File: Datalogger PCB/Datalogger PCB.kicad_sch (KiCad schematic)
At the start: 45 parts, among them J1 Conn_01x02_Pin, M1 Motor_Servo, M2 Motor_Servo, M3 Motor_Servo, M4 Motor_Servo, U1 Teensy4.1, U2 BNO055, U3 LPS25HB, U4 AMS1117-5.0, U5 NRF24L01_Breakout, U6 VN5E160STR-E, U7 VN5E160STR-E, U8 VN5E160STR-E, U9 VN5E160STR-E

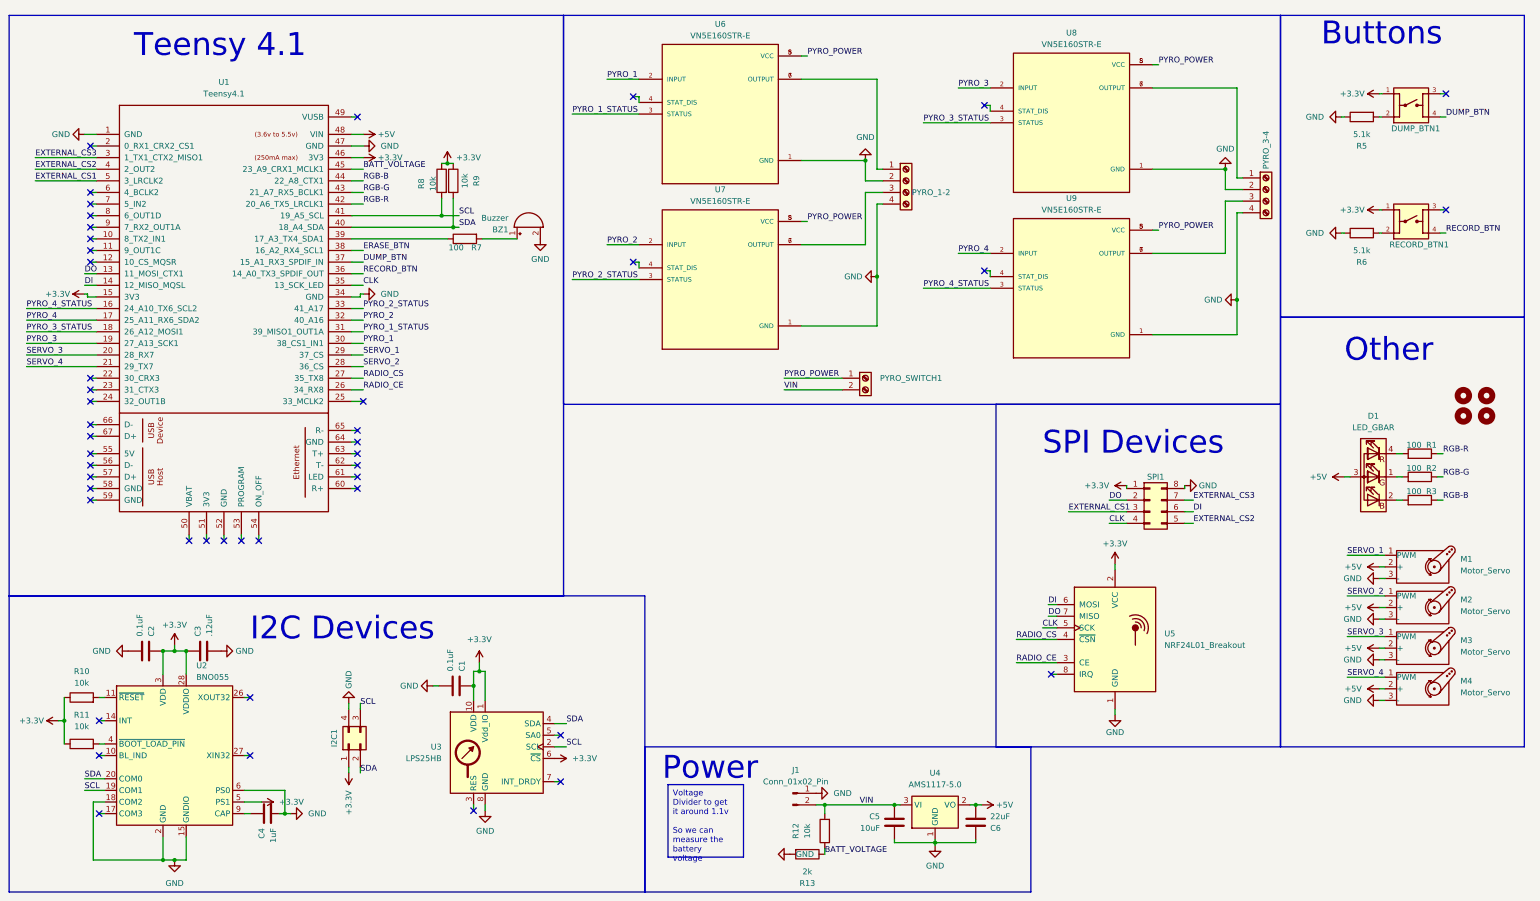
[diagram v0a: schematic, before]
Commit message: Added serial connector and power connectors
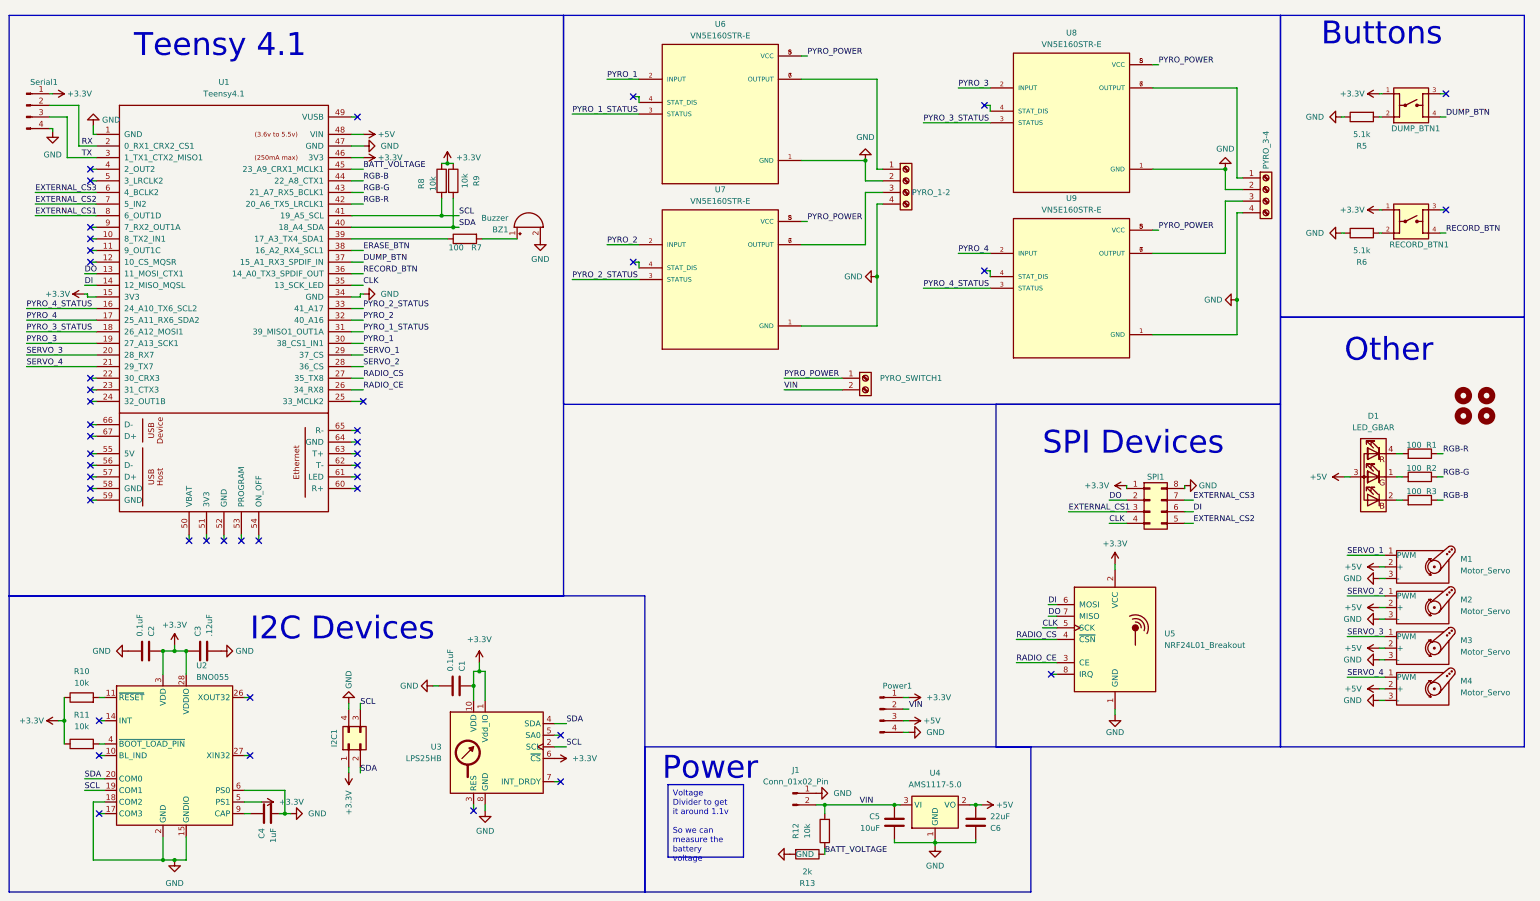
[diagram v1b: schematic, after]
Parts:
- added Power1, Serial1: Conn_01x04_Pin, Connector_PinHeader_1.27mm:PinHeader_1x04_P1.27mm_Vertical, symbol Connector:Conn_01x04_Pin
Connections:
- net +3.3V: now also Power1.1 (Pin_1), Serial1.1 (Pin_1)
- net +5V: now also Power1.3 (Pin_3)
- net EXTERNAL_CS1: now also U1.8 (6_OUT1D); no longer U1.5 (3_LRCLK2)
- net EXTERNAL_CS2: now also U1.7 (5_IN2); no longer U1.4 (2_OUT2)
- net EXTERNAL_CS3: now also U1.6 (4_BCLK2); no longer U1.3 (1_TX1_CTX2_MISO1)
- net GND: now also Power1.4 (Pin_4), Serial1.4 (Pin_4)
- net VIN: now also Power1.2 (Pin_2)
- net RX: now reaches U1.2 (0_RX1_CRX2_CS1)
- net RX: now also Serial1.2 (Pin_2)
- new net TX: Serial1.3 (Pin_3), U1.3 (1_TX1_CTX2_MISO1)
- no-connect marks 46 -> 44

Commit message: Remove DUMP_BTN
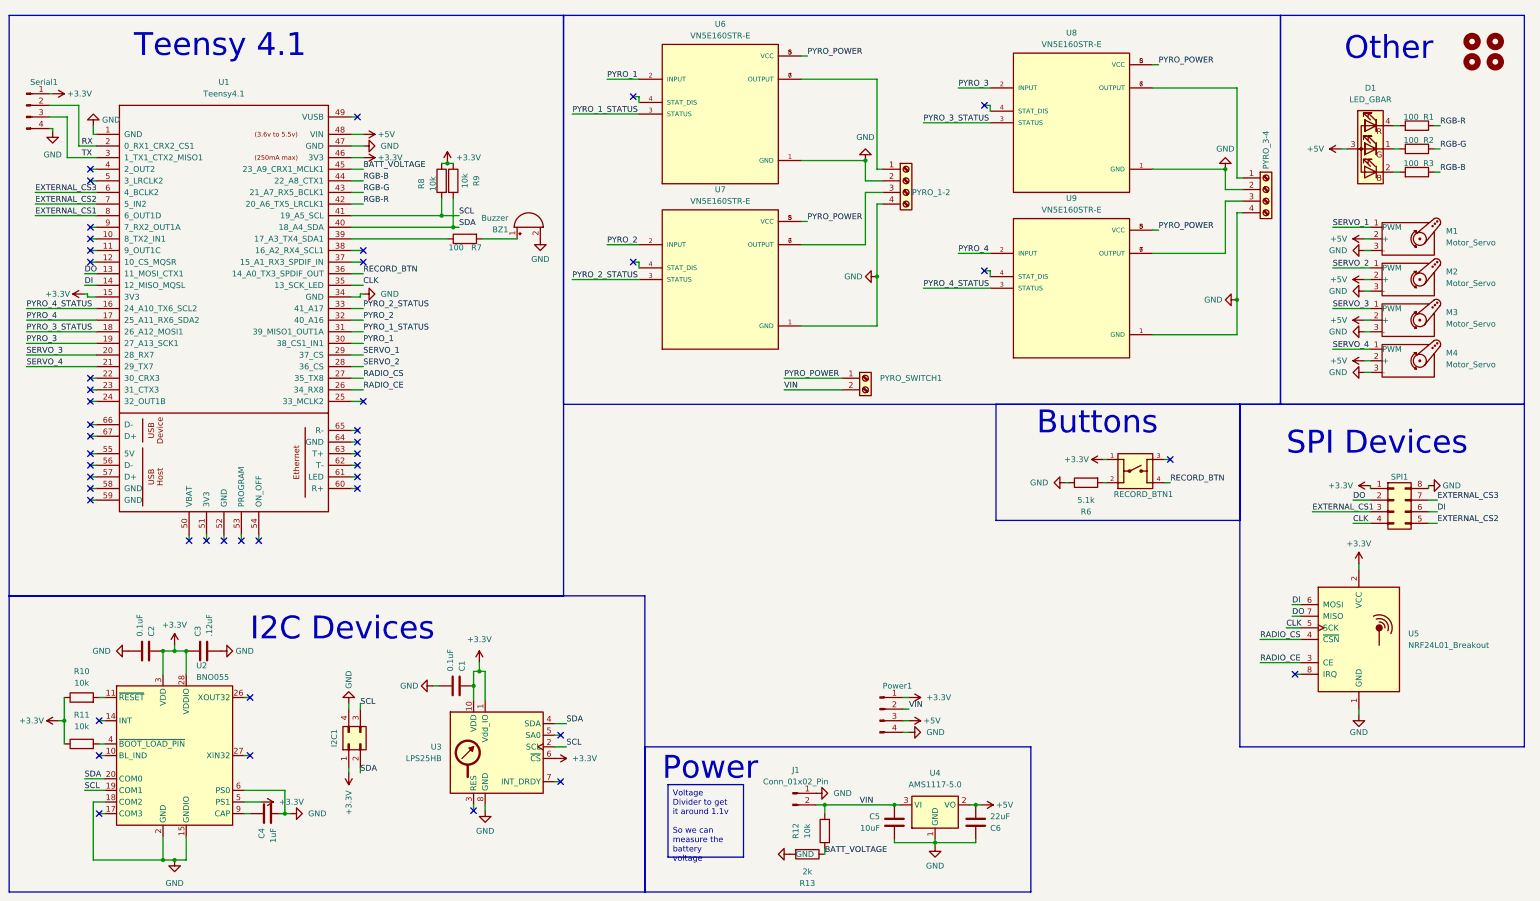
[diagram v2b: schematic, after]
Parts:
- removed DUMP_BTN1: FSM8JH, Push Button:SW_FSM8JH, symbol Push Button:FSM8JH
- removed R5: 5.1k, Resistor_SMD:R_0603_1608Metric_Pad0.98x0.95mm_HandSolder, symbol Device:R
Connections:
- net DUMP_BTN: no longer names the net of U1.37 (15_A1_RX3_SPDIF_IN)
- net ERASE_BTN: no longer names the net of U1.38 (16_A2_RX4_SCL1)
- no-connect marks 44 -> 45
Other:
- moved on the sheet: D1, M1, M2, M3, M4, R1, R2, R3, R6, RECORD_BTN1, SPI1, U5

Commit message: Final Revision
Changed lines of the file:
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@@
     (stroke (width 0) (type default))
   )
-  (wire (pts (xy 88.9 162.56) (xy 88.9 163.83))
+  (wire (pts (xy 88.9 162.814) (xy 88.9 163.83))
     (stroke (width 0) (type default))
   )
@@
     (effects (font (size 1.27 1.27)) (justify left bottom))
   )
-  (label "SCL" (at 88.9 163.195 0) (fields_autoplaced)
-    (effects (font (size 1.27 1.27)) (justify left bottom))
-  )
+  (label "SCL" (at 88.9 162.814 0) (fields_autoplaced)
+    (effects (font (size 1.27 1.27)) (justify left bottom))
+  )

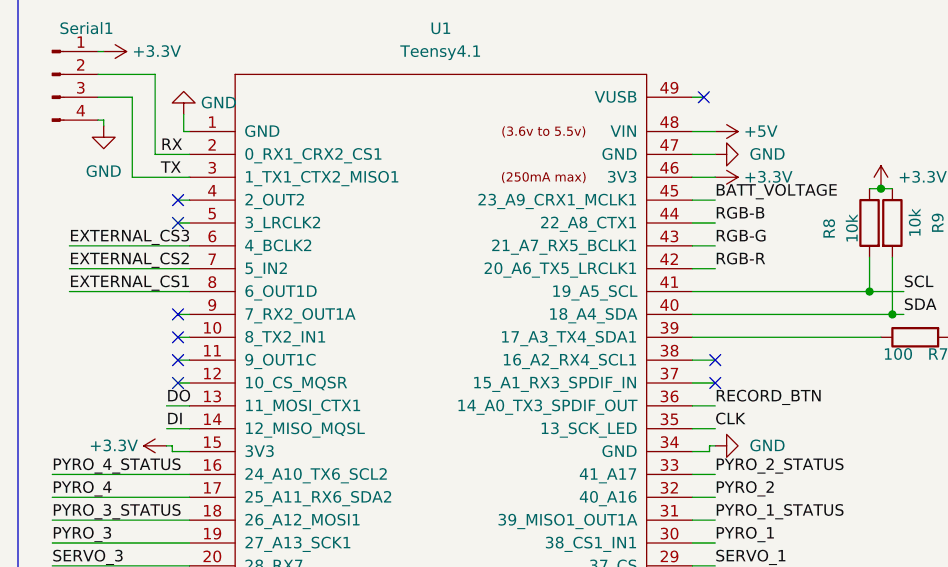
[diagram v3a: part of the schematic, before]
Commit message: Made LED's connected to PWM pins
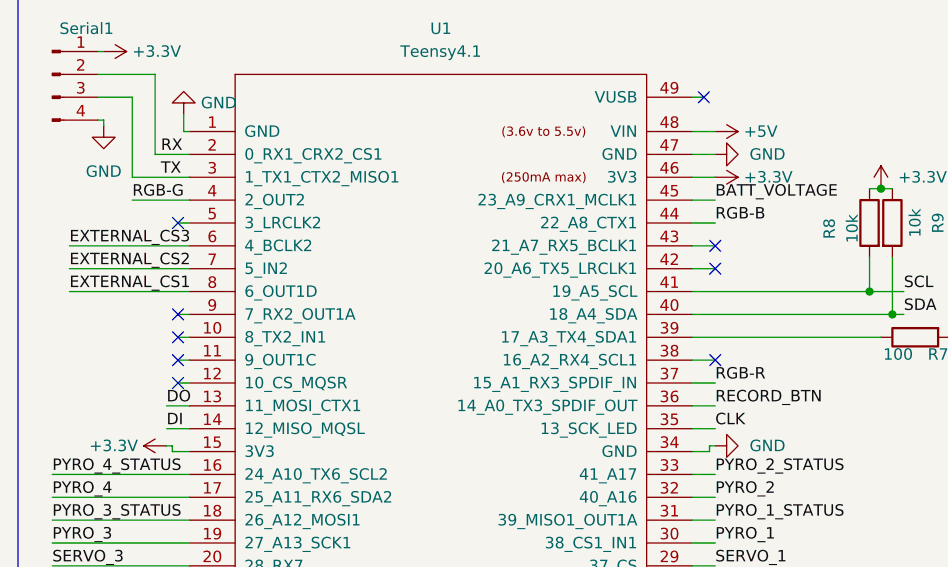
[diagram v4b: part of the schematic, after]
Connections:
- net RGB-G: now also U1.4 (2_OUT2); no longer U1.43 (21_A7_RX5_BCLK1)
- net RGB-R: now also U1.37 (15_A1_RX3_SPDIF_IN); no longer U1.42 (20_A6_TX5_LRCLK1)
